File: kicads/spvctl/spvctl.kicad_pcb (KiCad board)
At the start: 2 copper layers, 57.1 x 25.4 mm, 15 parts, among them J1 V+, J2 V-, J3 PV, J4 V+, J5 V-, J6 PV, J7 GND, J8 GND

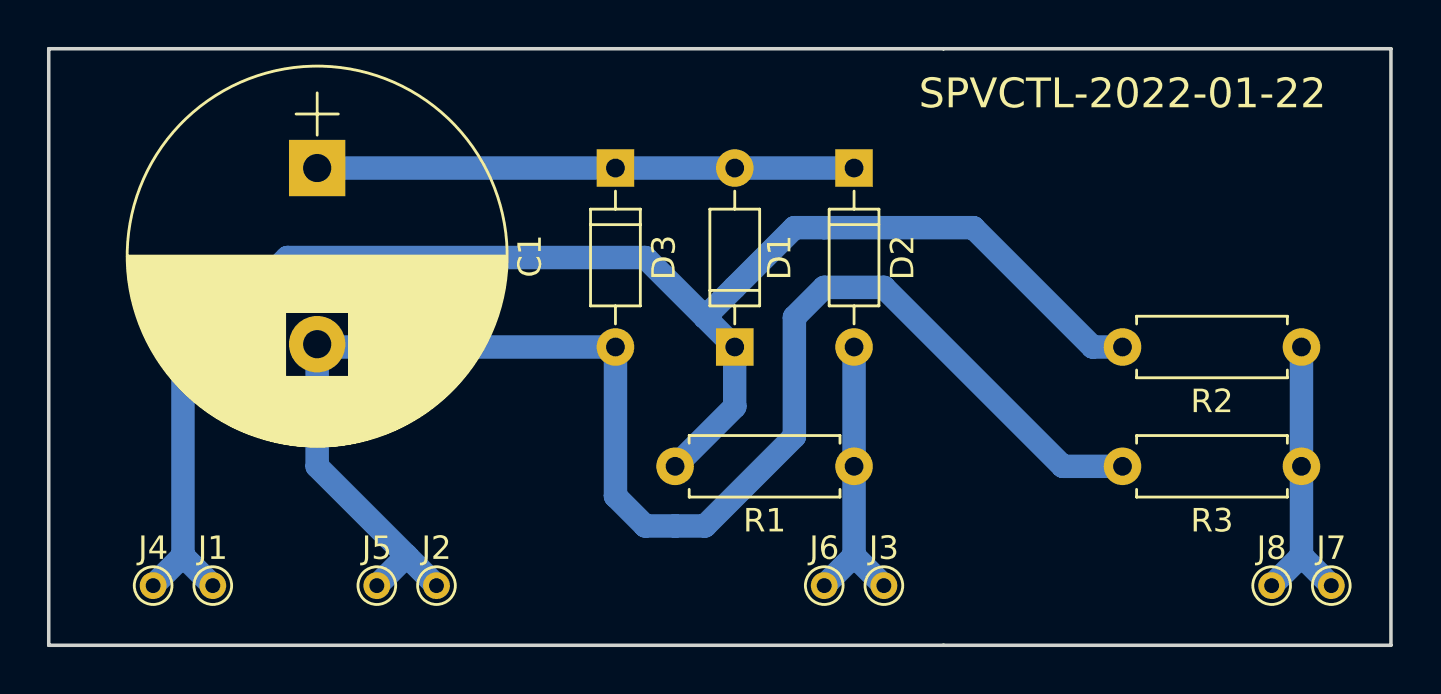
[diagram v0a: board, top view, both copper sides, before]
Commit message: update manually generated pcbs to include patches and logo
BACKPLANE 2024-04-17
EIGHT 2024-04-17
IOW100PADDLE 2024-04-25
SPVCTL 2024-04-17
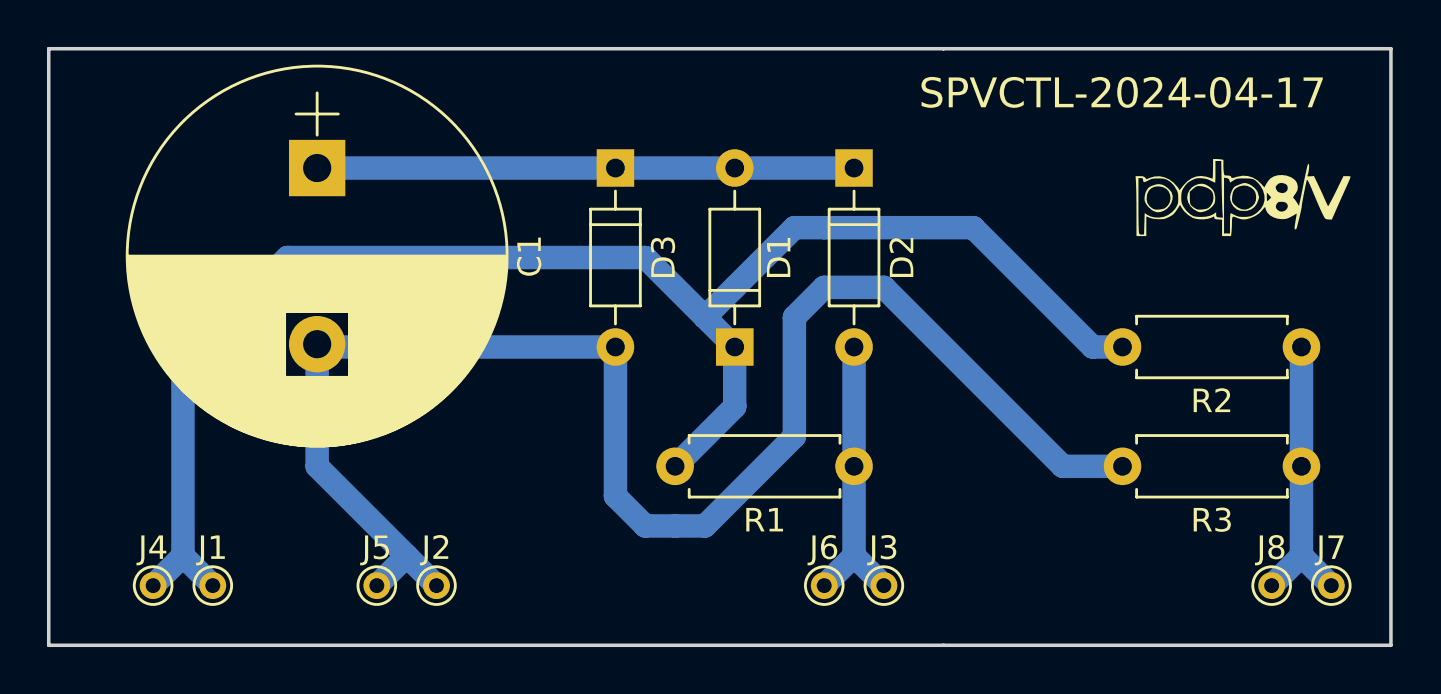
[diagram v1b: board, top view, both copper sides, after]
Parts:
- added G***: LOGO, LOGO, F.Cu at (50.8, 6.35)
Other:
- net class Default removed
- rule pad_to_mask_clearance: 0.2 -> 0
- board text added: "SPVCTL-2024-04-17"
- board text removed: "SPVCTL-2022-01-22"
